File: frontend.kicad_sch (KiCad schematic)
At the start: 113 parts, among them J1 RFIN, U10 ADA4938-1, U5 TLV77333PDBVR, U6 AD9515, U7 ADL5206, U8 AP2205-50Y-13, U9 AP2205-50Y-13

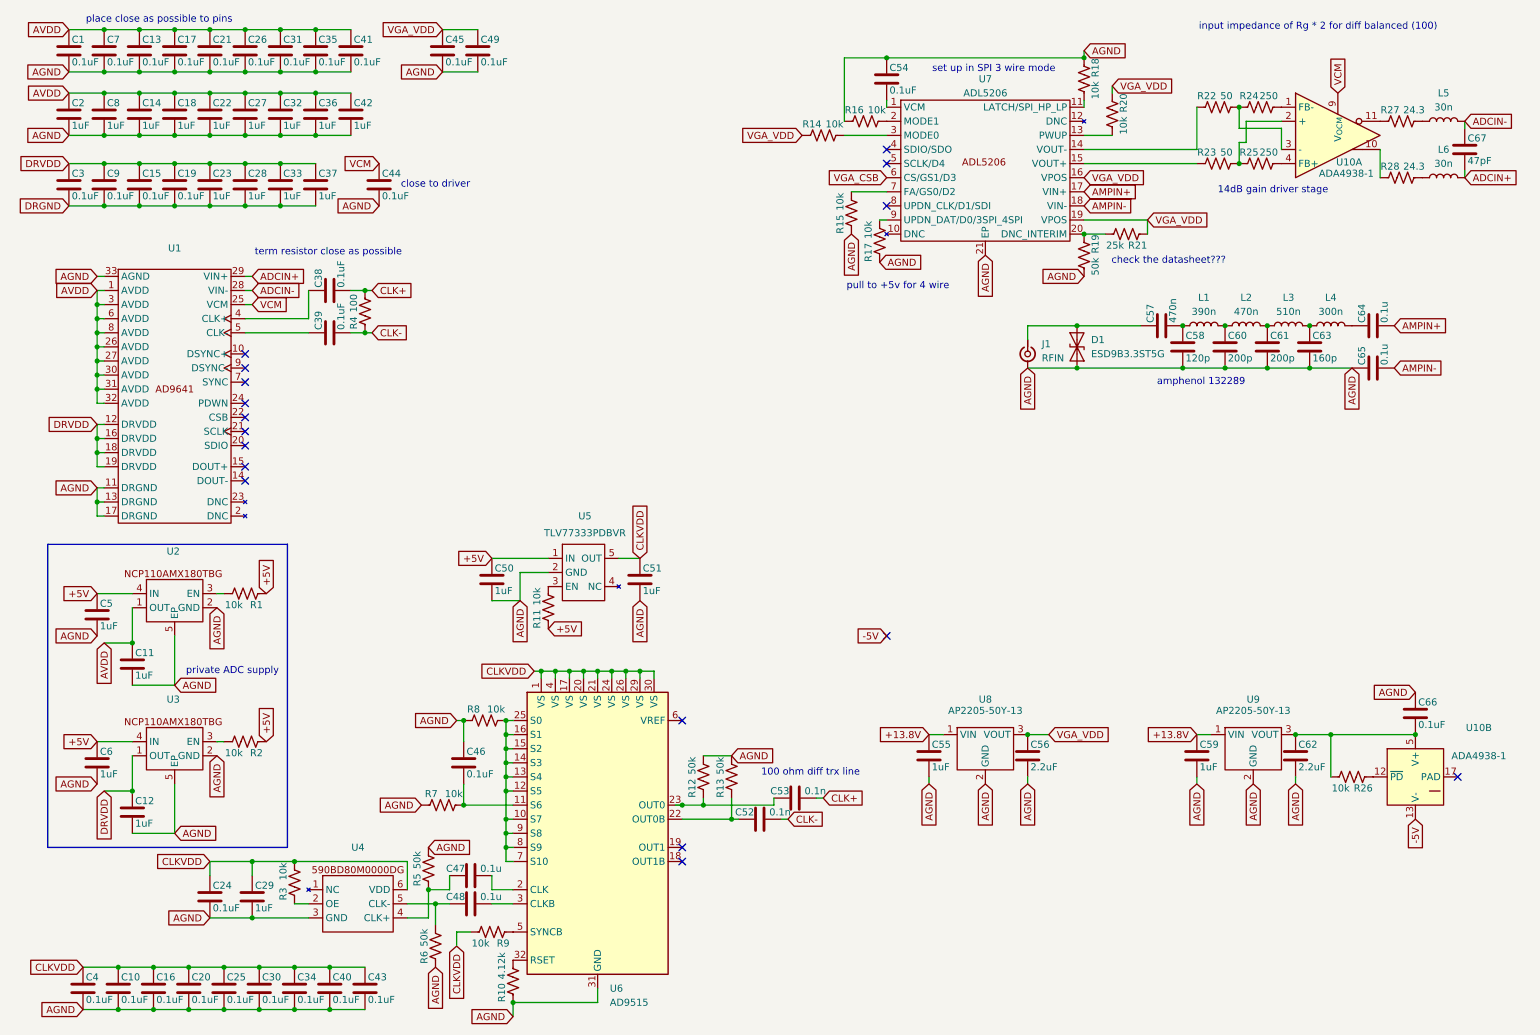
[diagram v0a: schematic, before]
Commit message: adc crashout complete
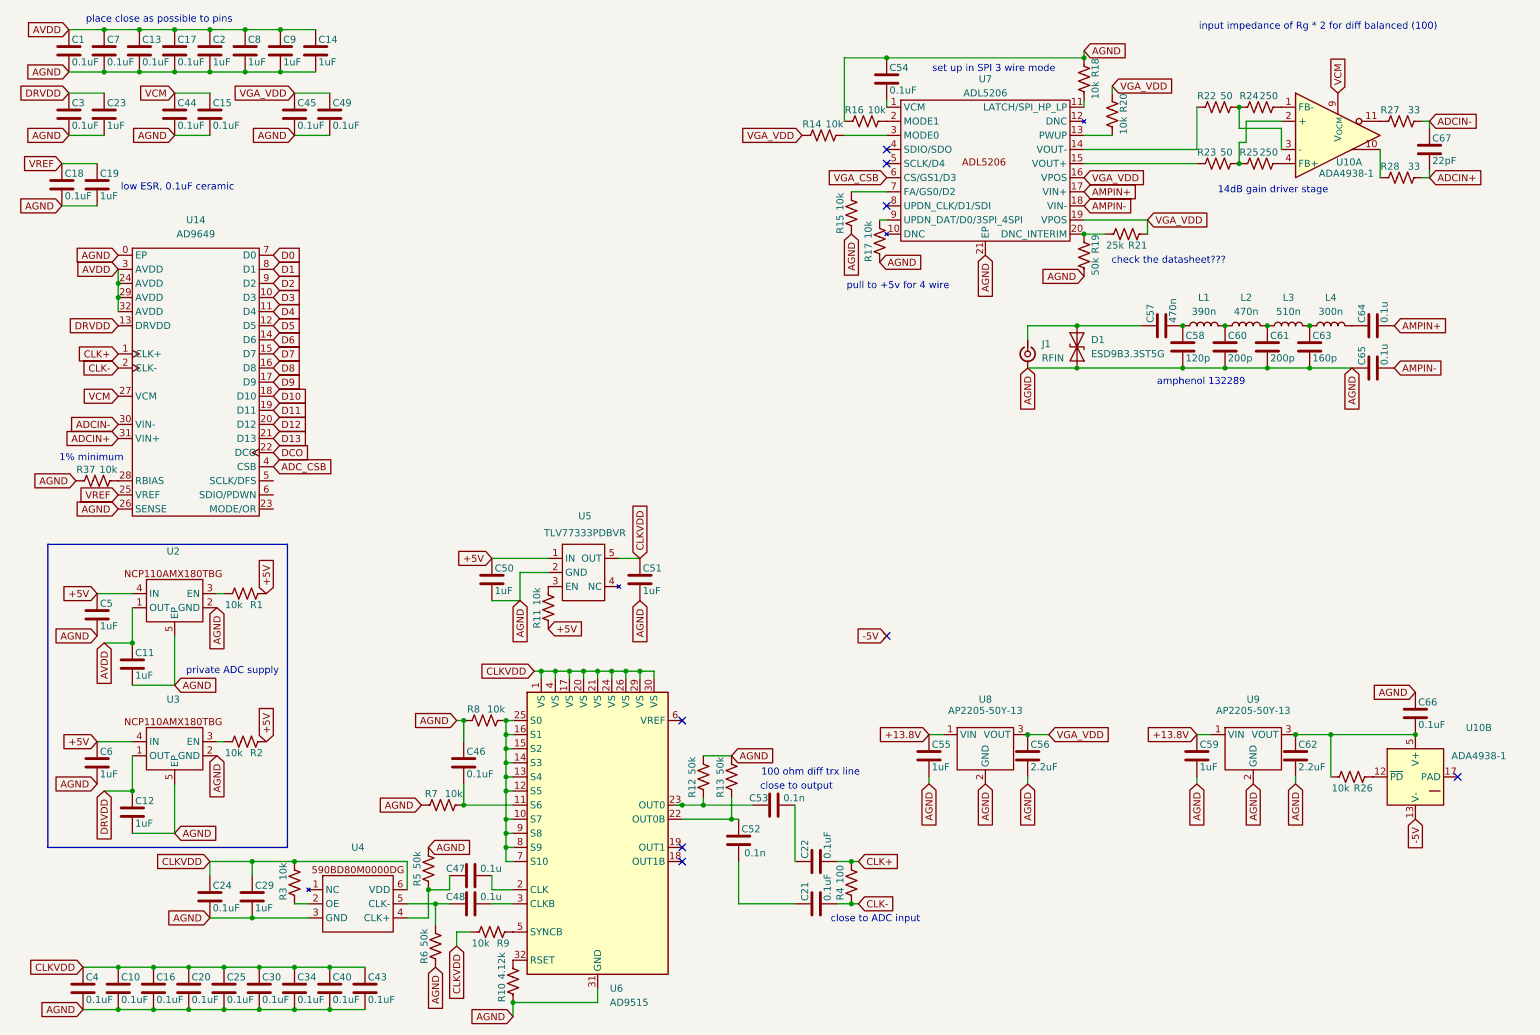
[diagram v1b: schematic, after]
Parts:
- removed C26, C31, C35, C38, C39, C41: 0.1uF, Capacitor_SMD:C_0402_1005Metric, symbol Device:C
- removed C27, C28, C32, C33, C36, C37, C42: 1uF, Capacitor_SMD:C_0402_1005Metric, symbol Device:C
- removed L5, L6: 30n, Inductor_SMD:L_0402_1005Metric, symbol Device:L
- removed U1: ~, Package_CSP:LFCSP-32-1EP_5x5mm_P0.5mm_EP3.6x3.6mm_ThermalVias, symbol hfsdr:AD9641
- added R37: 10k, Resistor_SMD:R_0402_1005Metric, symbol Device:R_US
- added U14: AD9649, Package_CSP:LFCSP-32-1EP_5x5mm_P0.5mm_EP3.5x3.5mm, symbol hfsdr:AD9649
- C18, C22: value 1uF -> 0.1uF
- C19, C9: value 0.1uF -> 1uF
- C67: value 47pF -> 22pF
- R27, R28: value 24.3 -> 33
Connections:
- net DRGND is gone; now on net AGND: C15.2, C19.2, C23.2, C3.2, C9.2
- net ADCIN+: now also R28.2, U14.31 (VIN+)
- net ADCIN-: now also R27.2, U14.30 (VIN-)
- net AGND: now also R37.1, U14.0 (EP), U14.26 (SENSE); no longer C21.2, C22.2
- net AVDD: now also C9.1, U14.24 (AVDD), U14.29 (AVDD), U14.3 (AVDD), U14.32 (AVDD); no longer C18.1, C21.1, C22.1
- net CLK+: now also C22.2, U14.1 (CLK+); no longer C53.2
- net CLK-: now also C21.2, U14.2 (CLK-); no longer C52.2
- net DRVDD: now also U14.13 (DRVDD); no longer C15.1, C19.1, C9.1
- net VCM: now also C15.1, U14.27 (VCM)
- new net: R37.2, U14.28 (RBIAS)
- new net: C21.1, C52.2
- new net: C22.1, C53.2
- new net ADC_CSB: U14.4 (CSB)
- new net D0: U14.7 (D0)
- new net D1: U14.8 (D1)
- new net D10: U14.18 (D10)
- new net D11: U14.19 (D11)
- new net D12: U14.20 (D12)
- new net D13: U14.21 (D13)
- new net D2: U14.9 (D2)
- new net D3: U14.10 (D3)
- new net D4: U14.11 (D4)
- new net D5: U14.12 (D5)
- new net D6: U14.14 (D6)
- new net D7: U14.15 (D7)
- new net D8: U14.16 (D8)
- new net D9: U14.17 (D9)
- new net DCO: U14.22 (DCO)
- new net VREF: C18.1, C19.1, U14.25 (VREF)
- no-connect marks 17 -> 8
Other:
- note added: "1% minimum"
- note added: "close to ADC input"
- note added: "close to output"
- note added: "low ESR, 0.1uF ceramic"
- note removed: "close to driver"
- note removed: "term resistor close as possible"
- moved on the sheet: C23, C3, C44, C45, C49, C52, C53, C67

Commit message: some more fpga work
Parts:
- removed U4: ~, hfsdr:SI590_5x7mm, symbol hfsdr:590BD80M0000DG
- added Y1: 590ND595M000DG, 590ND595M000DG, symbol hfsdr:590ND595M000DG
- renumbered J1 to RF1
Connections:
- net AGND: now also Y1.3 (GND)
- net CLKVDD: now also Y1.6 (VDD)
- net at C47.1, R5.1: now also Y1.4 (CLK+)
- net at R3.1: now also Y1.2 (OE)
- net at C48.1, R6.2: now also Y1.5 (CLK-)
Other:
- moved on the sheet: C24, C29, R3

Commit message: i dont even remember what i did
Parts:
- added C117: 1000p, Capacitor_SMD:C_0402_1005Metric, symbol Device:C
- Y1: value 590ND595M000DG -> 590BD80M0000DG; footprint 590ND595M000DG -> hfsdr:590BD80M0000DG; Manufacturer_Part_Number 590ND595M000DG -> 590BD80M0000DG; Mouser Part Number 634-590ND595M000DG -> (none); Mouser Price/Stock https://www.mouser.co.uk/ProductDetail/Skyworks-Solutions-I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 -> (none)
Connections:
- net -5V is gone; now on net AGND: U10.13 (V-), U10.14 (V-), U10.15 (V-), U10.16 (V-)
- net AGND: now also U10.17 (PAD), U14.33 (EP), C117.1; no longer U14.0 (EP)
- net VGA_VDD: no longer R20.1
- net at R22.2, R24.1: now also U10.2 (+); no longer U10.3 (-)
- net VGA_SDIO: now reaches U7.4 (SDIO/SDO)
- net VGA_SCLK: now reaches U7.5 (SCLK/D4)
- net at R23.2, R25.1: now also U10.3 (-); no longer U10.2 (+)
- net ADC_MODE/OR: now reaches U14.23 (MODE/OR)
- net ADC_SCLK: now reaches U14.5 (SCLK/DFS)
- net ADC_SDIO: now reaches U14.6 (SDIO/PDWN)
- net at C62.1, C66.2, R26.2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: now also C117.2
- new net VGA_ENABLE: R20.1
- no-connect marks 8 -> 4
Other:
- note removed: "private ADC supply"

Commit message: some moderate pcb work
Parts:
- removed R20, R3, R7, R8: 10k, Resistor_SMD:R_0402_1005Metric, symbol Device:R_US
- added C126: 0.1uF, Capacitor_SMD:C_0402_1005Metric, symbol Device:C
- U10: footprint Package_CSP:LFCSP-16-1EP_3x3mm_P0.5mm_EP1.3x1.3mm_ThermalVias -> Package_CSP:LFCSP-16-1EP_3x3mm_P0.5mm_EP1.3x1.3mm
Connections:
- net AGND: now also U6.10 (S7), U6.12 (S5), U6.13 (S4), U6.14 (S3), U6.15 (S2), U6.16 (S1), U6.25 (S0), U6.7 (S10), U6.8 (S9), U6.9 (S8), C126.2
- net CLKVDD: now also C46.2, U6.11 (S6), C126.1
- net VGA_ENABLE: now also U7.13 (PWUP)
- net at R22.1: now also U7.15 (VOUT+); no longer U7.14 (VOUT-)
- net at R23.1: now also U7.14 (VOUT-); no longer U7.15 (VOUT+)
- no-connect marks 4 -> 5
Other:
- moved on the sheet: C24, C29, C46

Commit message: i forgot
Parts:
- added C127, C129, C130: 1n, Capacitor_SMD:C_0402_1005Metric, symbol Device:C
- added C128, C131, C132: 0.1u, Capacitor_SMD:C_0402_1005Metric, symbol Device:C
- C117: value 1000p -> 0.1u
- C66: value 0.1uF -> 1n
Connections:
- net AGND: now also C117.2, C66.2, C127.2, C128.2, C129.2, C130.2, C131.2, C132.2; no longer C117.1, C66.1
- net at C47.1, R5.1: now also Y1.5 (CLK-); no longer Y1.4 (CLK+)
- net DRIVER_VDD: now reaches C62.1, R26.2, U10.5 (V+), U10.6 (V+), U10.7 (V+), U10.8 (V+), U9.3 (VOUT)
- net DRIVER_VDD: now also C117.1, C66.1, C127.1, C128.1, C129.1, C130.1, C131.1, C132.1; no longer C117.2, C66.2
- net at C48.1, R6.2: now also Y1.4 (CLK+); no longer Y1.5 (CLK-)
